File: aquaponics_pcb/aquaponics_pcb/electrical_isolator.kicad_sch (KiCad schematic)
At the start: 11 parts, among them IC3 ADM3260ARSZ, Q2 SSM6N35AFE,LF

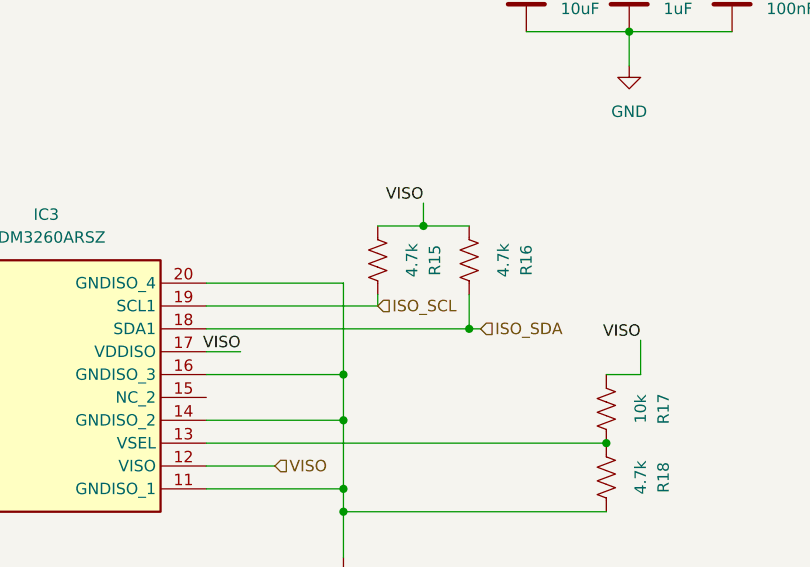
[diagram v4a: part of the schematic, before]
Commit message: finish ground and power pours. fix rules and run final DRC. export gerbers
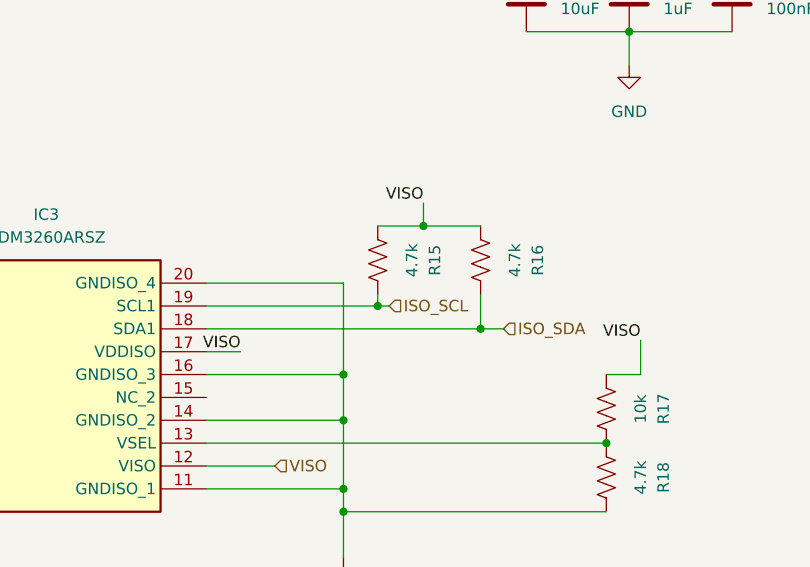
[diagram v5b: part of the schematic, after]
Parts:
- C10: JLCPCB Part # (none) -> C15849; LCSC Part Number (none) -> C15849
- C11: JLCPCB Part # (none) -> C14663; LCSC Part Number (none) -> C14663
- C9: JLCPCB Part # (none) -> C194427; LCSC Part Number (none) -> C194427
- R13, R14: JLCPCB Part # (none) -> C22935; LCSC Part Number (none) -> C22935
- R15, R16, R18: JLCPCB Part # (none) -> C99782; LCSC Part Number (none) -> C99782
- R17: JLCPCB Part # (none) -> C98220; LCSC Part Number (none) -> C98220
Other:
- moved on the sheet: R16
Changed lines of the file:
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@@
-	)
-	(junction
-		(at 171.45 73.66)
-		(diameter 0)
-		(color 0 0 0 0)
 	)
 	(junction
@@
 	)
 	(junction
+		(at 161.29 71.12)
+		(diameter 0)
+		(color 0 0 0 0)
+	)
+	(junction
 		(at 157.48 93.98)
 		(diameter 0)
 		(color 0 0 0 0)
 	)
+	(junction
+		(at 172.72 73.66)
+		(diameter 0)
+		(color 0 0 0 0)
+	)
 	(wire
 		(pts
@@
 	(wire
 		(pts
-			(xy 171.45 69.85) (xy 171.45 73.66)
+			(xy 172.72 69.85) (xy 172.72 73.66)
 		)
 		(stroke
@@
 	(wire
 		(pts
-			(xy 172.72 73.66) (xy 171.45 73.66)
+			(xy 175.26 73.66) (xy 172.72 73.66)
 		)
 		(stroke
@@
 	(wire
 		(pts
-			(xy 171.45 62.23) (xy 166.37 62.23)
-		)
-		(stroke
-			(width 0)
-			(type default)
-		)
-	)
-	(wire
-		(pts
-			(xy 171.45 73.66) (xy 142.24 73.66)
+			(xy 172.72 62.23) (xy 166.37 62.23)
+		)
+		(stroke
+			(width 0)
+			(type default)
+		)
+	)
+	(wire
+		(pts
+			(xy 142.24 73.66) (xy 172.72 73.66)
 		)
 		(stroke
@@
 		(pts
 			(xy 68.58 93.98) (xy 64.77 93.98)
+		)
+		(stroke
+			(width 0)
+			(type default)
+		)
+	)
+	(wire
+		(pts
+			(xy 161.29 71.12) (xy 162.56 71.12)
 		)
 		(stroke
@@
 	(hierarchical_label "ISO_SDA"
 		(shape input)
-		(at 172.72 73.66 0)
+		(at 175.26 73.66 0)
 		(effects
 			(font
@@
 	(hierarchical_label "ISO_SCL"
 		(shape input)
-		(at 161.29 71.12 0)
+		(at 162.56 71.12 0)
 		(effects
 			(font
@@
 			)
 		)
+		(property "LCSC Part Number" ""
+			(at 106.68 68.58 0)
+			(effects
+				(font
+					(size 1.27 1.27)
+				)
+				(hide yes)
+			)
+		)
+		(property "JLCPCB Part #" ""
+			(at 106.68 68.58 0)
+			(effects
+				(font
+					(size 1.27 1.27)
+				)
+				(hide yes)
+			)
+		)
 		(pin "5"
 		)
@@
 		(property "Description" "Resistor, US symbol"
 			(at 74.93 86.36 0)
+			(effects
+				(font
+					(size 1.27 1.27)
+				)
+				(hide yes)
+			)
+		)
+		(property "LCSC Part Number" "C22935"
+			(at 74.93 86.36 90)
+			(effects
+				(font
+					(size 1.27 1.27)
+				)
+				(hide yes)
+			)
+		)
+		(property "JLCPCB Part #" "C22935"
+			(at 74.93 86.36 90)
 			(effects
 				(font
@@
 			)
 		)
+		(property "LCSC Part Number" "C194427"
+			(at 177.8 36.83 0)
+			(effects
+				(font
+					(size 1.27 1.27)
+				)
+				(hide yes)
+			)
+		)
+		(property "JLCPCB Part #" "C194427"
+			(at 177.8 36.83 0)
+			(effects
+				(font
+					(size 1.27 1.27)
+				)
+				(hide yes)
+			)
+		)
 		(pin "1"
 		)
@@
 	(symbol
 		(lib_id "Device:R_US")
-		(at 171.45 66.04 0)
+		(at 172.72 66.04 0)
 		(unit 1)
 		(exclude_from_sim no)
@@
 		(dnp no)
 		(property "Reference" "R16"
-			(at 177.8 66.04 90)
+			(at 179.07 66.04 90)
 			(effects
 				(font
@@
 		)
 		(property "Value" "4.7k"
-			(at 175.26 66.04 90)
+			(at 176.53 66.04 90)
 			(effects
 				(font
@@
 		)
 		(property "Footprint" "Resistor_SMD:R_0603_1608Metric_Pad0.98x0.95mm_HandSolder"
-			(at 172.466 66.294 90)
+			(at 173.736 66.294 90)
 			(effects
 				(font
@@
 		)
 		(property "Datasheet" "~"
-			(at 171.45 66.04 0)
+			(at 172.72 66.04 0)
 			(effects
 				(font
@@
 		)
 		(property "Description" "Resistor, US symbol"
-			(at 171.45 66.04 0)
+			(at 172.72 66.04 0)
+			(effects
+				(font
+					(size 1.27 1.27)
+				)
+				(hide yes)
+			)
+		)
+		(property "LCSC Part Number" "C99782"
+			(at 172.72 66.04 90)
+			(effects
+				(font
+					(size 1.27 1.27)
+				)
+				(hide yes)
+			)
+		)
+		(property "JLCPCB Part #" "C99782"
+			(at 172.72 66.04 90)
 			(effects
 				(font
@@
 		(property "Description" "Resistor, US symbol"
 			(at 68.58 90.17 0)
+			(effects
+				(font
+					(size 1.27 1.27)
+				)
+				(hide yes)
+			)
+		)
+		(property "LCSC Part Number" "C22935"
+			(at 68.58 90.17 90)
+			(effects
+				(font
+					(size 1.27 1.27)
+				)
+				(hide yes)
+			)
+		)
+		(property "JLCPCB Part #" "C22935"
+			(at 68.58 90.17 90)
 			(effects
 				(font
@@
 			)
 		)
+		(property "LCSC Part Number" "C15849"
+			(at 189.23 36.83 0)
+			(effects
+				(font
+					(size 1.27 1.27)
+				)
+				(hide yes)
+			)
+		)
+		(property "JLCPCB Part #" "C15849"
+			(at 189.23 36.83 0)
+			(effects
+				(font
+					(size 1.27 1.27)
+				)
+				(hide yes)
+			)
+		)
 		(pin "1"
 		)
@@
 		(property "Description" "Resistor, US symbol"
 			(at 186.69 82.55 0)
+			(effects
+				(font
+					(size 1.27 1.27)
+				)
+				(hide yes)
+			)
+		)
+		(property "LCSC Part Number" "C98220"
+			(at 186.69 82.55 90)
+			(effects
+				(font
+					(size 1.27 1.27)
+				)
+				(hide yes)
+			)
+		)
+		(property "JLCPCB Part #" "C98220"
+			(at 186.69 82.55 90)
 			(effects
 				(font
@@
 			)
 		)
+		(property "LCSC Part Number" ""
+			(at 86.36 93.98 0)
+			(effects
+				(font
+					(size 1.27 1.27)
+				)
+				(hide yes)
+			)
+		)
+		(property "JLCPCB Part #" ""
+			(at 86.36 93.98 0)
+			(effects
+				(font
+					(size 1.27 1.27)
+				)
+				(hide yes)
+			)
+		)
 		(pin "6"
 		)
@@
 			)
 		)
+		(property "LCSC Part Number" "C14663"
+			(at 200.66 36.83 0)
+			(effects
+				(font
+					(size 1.27 1.27)
+				)
+				(hide yes)
+			)
+		)
+		(property "JLCPCB Part #" "C14663"
+			(at 200.66 36.83 0)
+			(effects
+				(font
+					(size 1.27 1.27)
+				)
+				(hide yes)
+			)
+		)
 		(pin "1"
 		)
@@
 			)
 		)
+		(property "LCSC Part Number" "C99782"
+			(at 161.29 66.04 90)
+			(effects
+				(font
+					(size 1.27 1.27)
+				)
+				(hide yes)
+			)
+		)
+		(property "JLCPCB Part #" "C99782"
+			(at 161.29 66.04 90)
+			(effects
+				(font
+					(size 1.27 1.27)
+				)
+				(hide yes)
+			)
+		)
 		(pin "1"
 		)
@@
 			(effects
 				(font
+					(size 1.27 1.27)
+				)
+				(hide yes)
+			)
+		)
+		(property "LCSC Part Number" "C99782"
+			(at 186.69 90.17 90)
+			(effects
+				(font
+					(size 1.27 1.27)
+				)
+				(hide yes)
+			)
+		)
+		(property "JLCPCB Part #" "C99782"
+			(at 186.69 90.17 90)
+			(effects
+				(font
